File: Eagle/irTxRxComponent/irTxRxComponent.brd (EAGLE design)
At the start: 99.3 x 25.7 mm, 10 parts, among them J20 Pixel, J22 IR Rx, Q2 2N5088

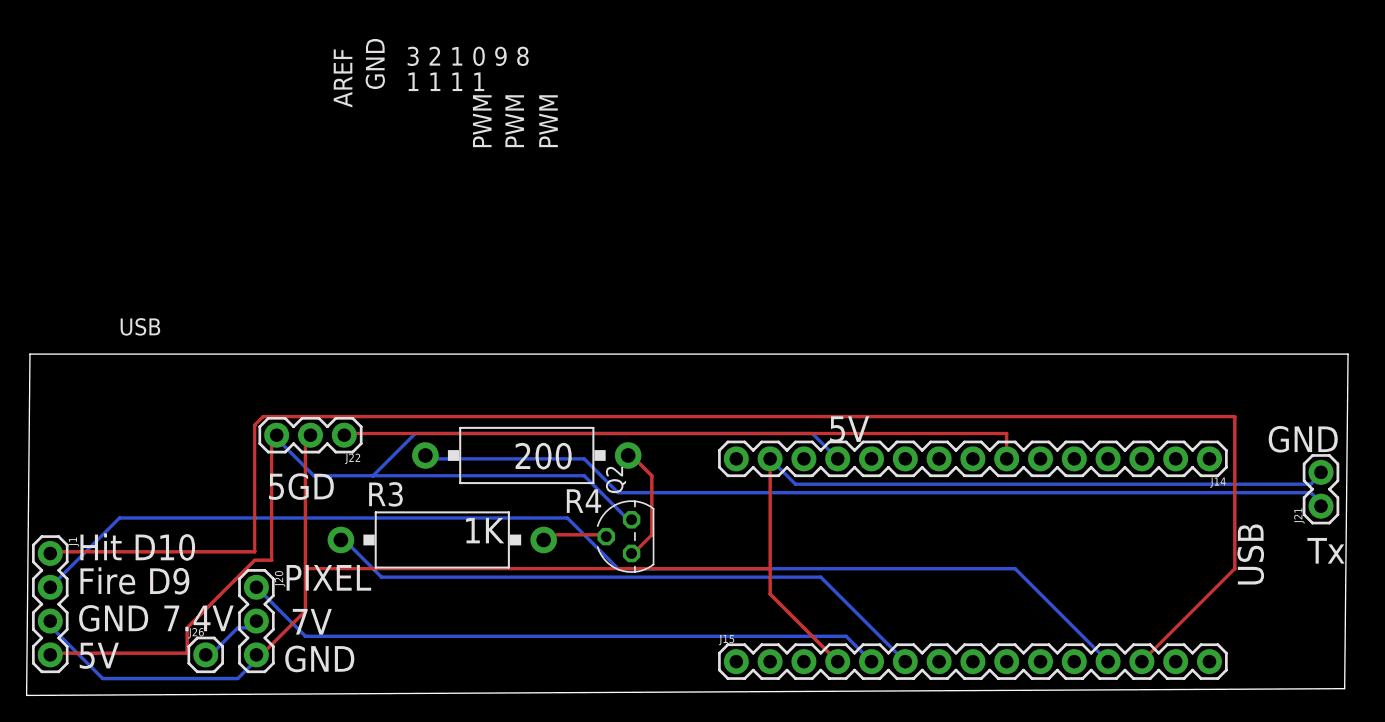
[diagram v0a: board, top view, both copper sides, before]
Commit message: Added Chrome App
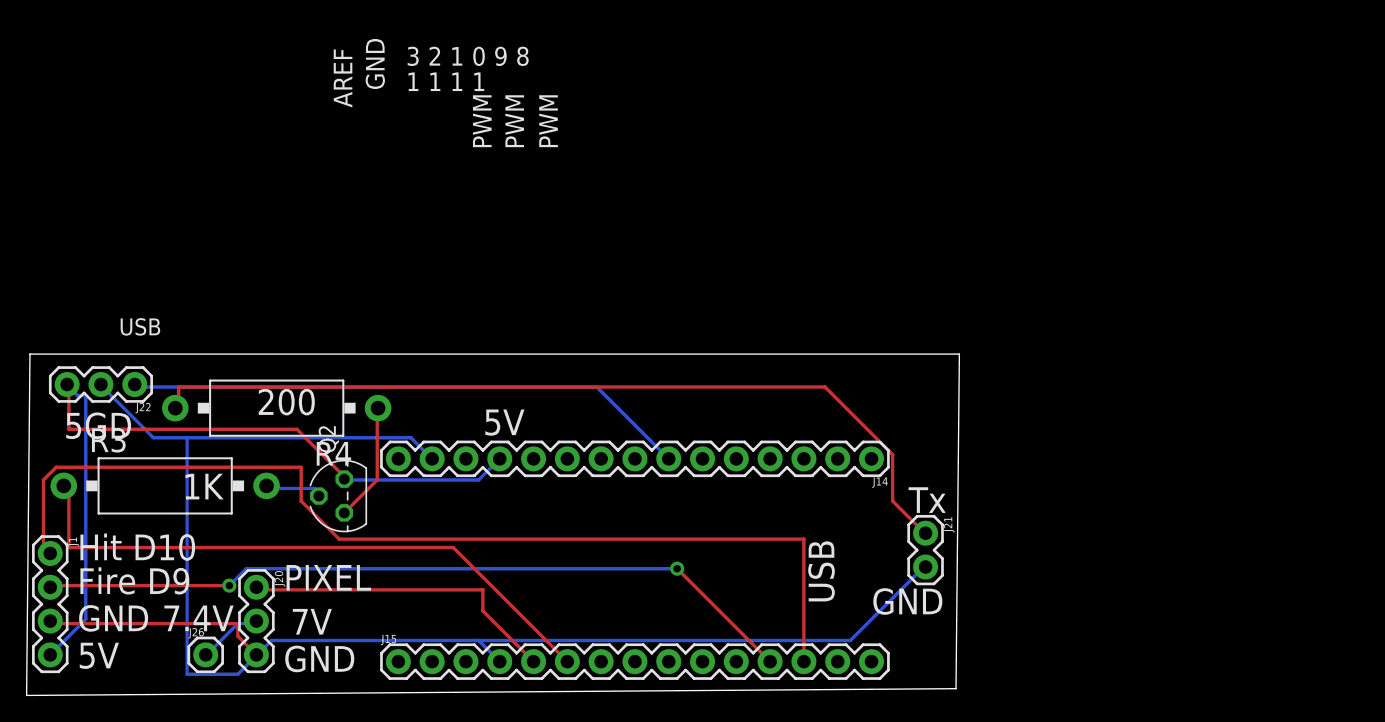
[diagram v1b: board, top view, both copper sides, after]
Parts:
- moved J21 29.8 mm to (67.6, 12.2), turned to 270 degrees
- moved J14 25.4 mm to (63.5, 17.8)
- moved J15 25.4 mm to (27.9, 2.54)
- moved Q2 21.8 mm to (23.9, 15.0)
- moved R3 21.2 mm to (10.4, 15.7)
- moved R4 19.1 mm to (18.8, 21.6)
- moved J22 16.2 mm to (8.13, 23.4)
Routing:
- net HIT: track 120.2 -> 76.2 mm
- net VCC_B: track 96.6 -> 60.5 mm
- net FIRE: track 86.1 -> 57.6 mm, vias 0 -> 2
- net D2_B: track 48.5 -> 24.1 mm
- net IRRX_B: track 51.7 -> 42.5 mm
- net GND_B: track 131.6 -> 123.2 mm
- net TX_C: track 69.0 -> 64.6 mm
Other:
- board size 99.3 x 25.7 mm -> 70.1 x 25.7 mm
